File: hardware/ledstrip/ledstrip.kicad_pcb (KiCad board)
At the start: 4 copper layers, 107 x 107.5 mm, 144 parts, among them J1 Conn_ARM_JTAG_SWD_10, J2 USB_C_Receptacle_USB2.0_16P, J4 BMS connectors, J5 Ledstrip connector, J6 Header for STUSB4500 I2C, Q1 Q_NMOS, Q10 Q_PMOS, Q11 Q_NMOS, Q2 Q_NMOS, Q3 Q_NMOS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

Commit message: Fix DRC
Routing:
- net Net-(SW1-B): track 0.43 -> 3.57 mm
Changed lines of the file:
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@@
 		(tags "capacitor")
 		(property "Reference" "C24"
-			(at 0 -1.43 270)
+			(at 0 1.4008 270)
 			(layer "F.SilkS")
 			(effects
@@
 		(layer "F.Cu")
 		(net 116)
+	)
+	(segment
+		(start 182.2927 109.8569)
+		(end 182.5752 110.1394)
+		(width 0.2)
+		(layer "F.Cu")
+		(net 116)
+	)
+	(segment
+		(start 179.5526 109.8569)
+		(end 182.2927 109.8569)
+		(width 0.2)
+		(layer "F.Cu")
+		(net 116)

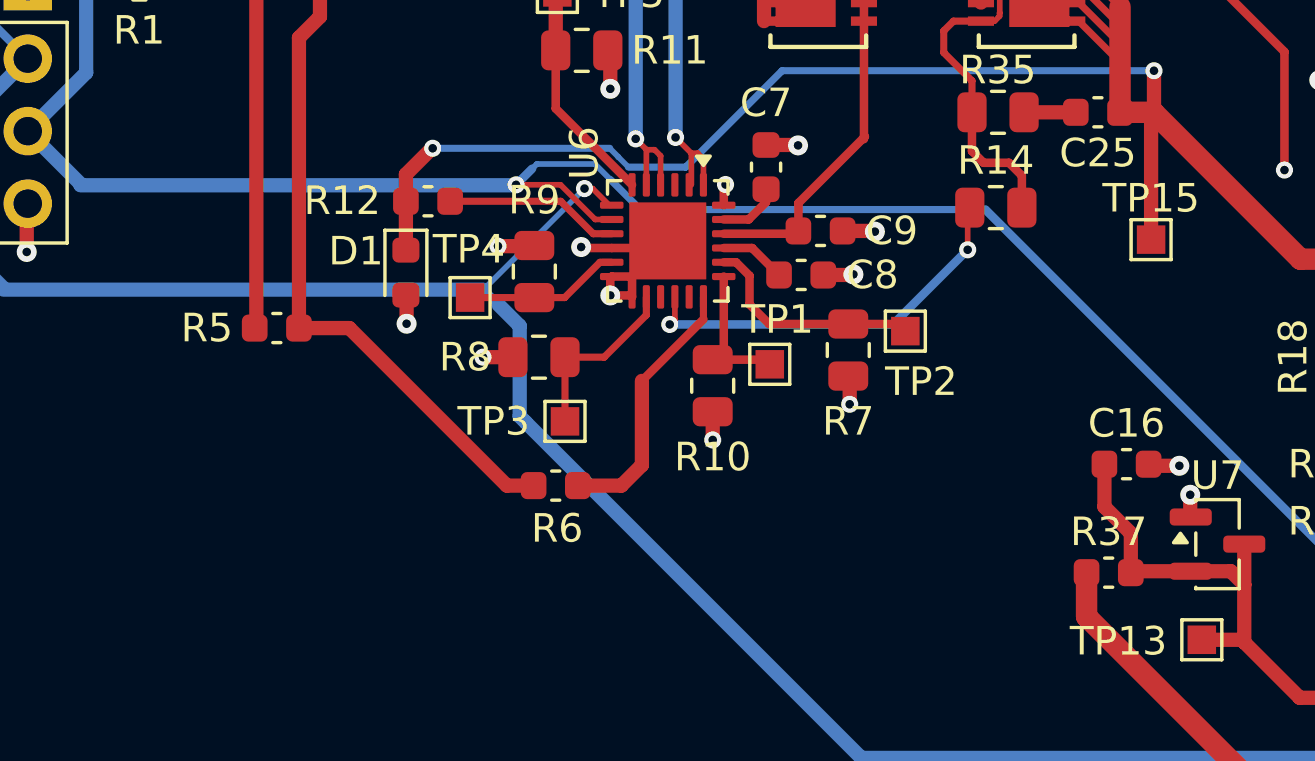
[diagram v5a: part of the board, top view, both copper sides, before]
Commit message: Fix wrong footprint (C_0603 instead of R_0603)
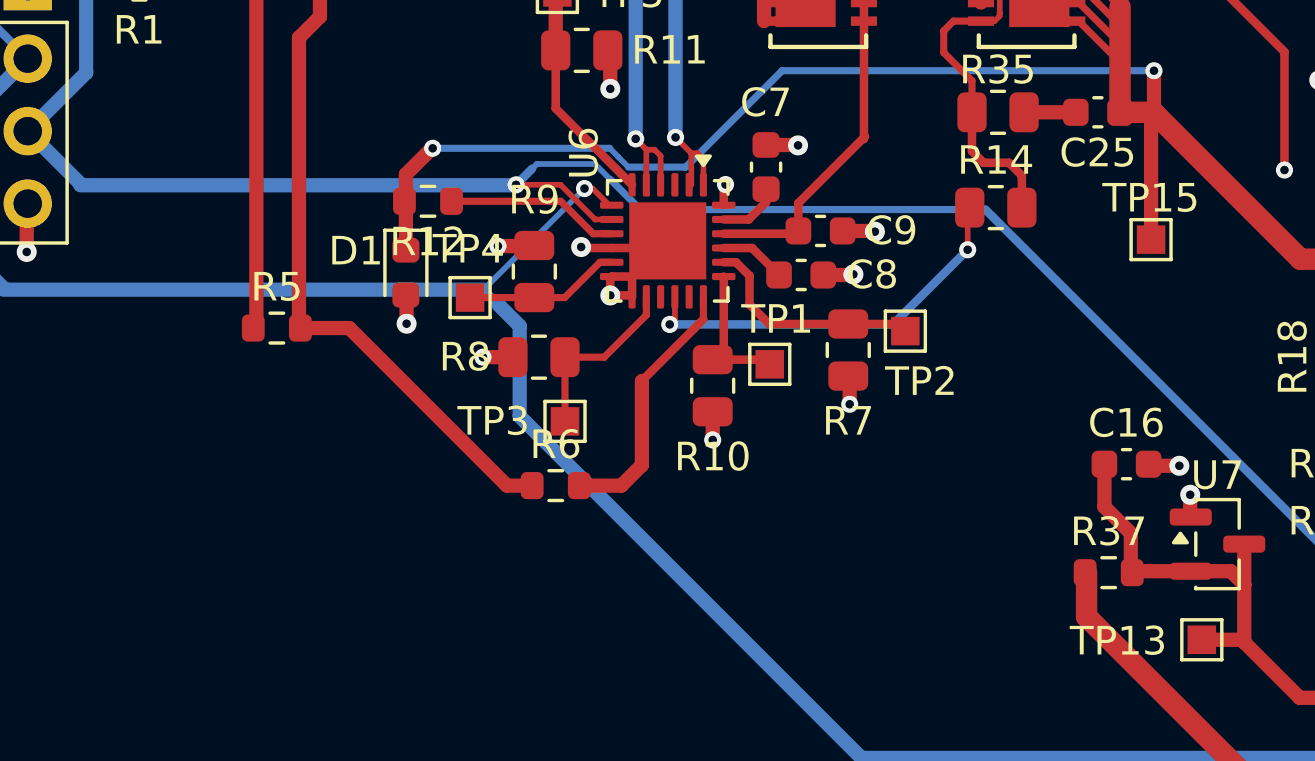
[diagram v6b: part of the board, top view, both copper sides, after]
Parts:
- R12, R37, R5, R6: footprint Capacitor_SMD:C_0603_1608Metric -> Resistor_SMD:R_0603_1608Metric
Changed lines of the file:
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@@
 		)
 	)
-	(footprint "Capacitor_SMD:C_0603_1608Metric"
+	(footprint "Resistor_SMD:R_0603_1608Metric"
 		(layer "F.Cu")
 		(at 119.5 131.25)
-		(descr "Capacitor SMD 0603 (1608 Metric), square (rectangular) end terminal, IPC-7351 nominal, (Body size source: IPC-SM-782 page 76, https://www.pcb-3d.com/wordpress/wp-content/uploads/ipc-sm-782a_amendment_1_and_2.pdf), generated with kicad-footprint-generator")
-		(tags "capacitor")
+		(descr "Resistor SMD 0603 (1608 Metric), square (rectangular) end terminal, IPC-7351 nominal, (Body size source: IPC-SM-782 page 72, https://www.pcb-3d.com/wordpress/wp-content/uploads/ipc-sm-782a_amendment_1_and_2.pdf), generated with kicad-footprint-generator")
+		(tags "resistor")
 		(property "Reference" "R6"
-			(at 0.05 1.5 0)
+			(at 0 -1.43 0)
 			(layer "F.SilkS")
 			(effects
@@
 		(attr smd)
 		(fp_line
-			(start -0.14058 -0.51)
-			(end 0.14058 -0.51)
+			(start -0.237258 -0.5225)
+			(end 0.237258 -0.5225)
 			(stroke
 				(width 0.12)
@@
 		)
 		(fp_line
-			(start -0.14058 0.51)
-			(end 0.14058 0.51)
+			(start -0.237258 0.5225)
+			(end 0.237258 0.5225)
 			(stroke
 				(width 0.12)
@@
 		)
 		(fp_rect
-			(start -0.8 -0.4)
-			(end 0.8 0.4)
+			(start -0.8 -0.4125)
+			(end 0.8 0.4125)
 			(stroke
 				(width 0.1)
@@
 		)
 		(pad "1" smd roundrect
-			(at -0.775 0)
-			(size 0.9 0.95)
+			(at -0.825 0)
+			(size 0.8 0.95)
 			(layers "F.Cu" "F.Mask" "F.Paste")
 			(roundrect_rratio 0.25)
@@
 		)
 		(pad "2" smd roundrect
-			(at 0.775 0)
-			(size 0.9 0.95)
+			(at 0.825 0)
+			(size 0.8 0.95)
 			(layers "F.Cu" "F.Mask" "F.Paste")
 			(roundrect_rratio 0.25)
@@
 		)
 		(embedded_fonts no)
-		(model "${KICAD9_3DMODEL_DIR}/Capacitor_SMD.3dshapes/C_0603_1608Metric.step"
+		(model "${KICAD9_3DMODEL_DIR}/Resistor_SMD.3dshapes/R_0603_1608Metric.step"
 			(offset
 				(xyz 0 0 0)
@@
 		)
 	)
-	(footprint "Capacitor_SMD:C_0603_1608Metric"
+	(footprint "Resistor_SMD:R_0603_1608Metric"
 		(layer "F.Cu")
 		(at 115.025 121.2875 180)
-		(descr "Capacitor SMD 0603 (1608 Metric), square (rectangular) end terminal, IPC-7351 nominal, (Body size source: IPC-SM-782 page 76, https://www.pcb-3d.com/wordpress/wp-content/uploads/ipc-sm-782a_amendment_1_and_2.pdf), generated with kicad-footprint-generator")
-		(tags "capacitor")
+		(descr "Resistor SMD 0603 (1608 Metric), square (rectangular) end terminal, IPC-7351 nominal, (Body size source: IPC-SM-782 page 72, https://www.pcb-3d.com/wordpress/wp-content/uploads/ipc-sm-782a_amendment_1_and_2.pdf), generated with kicad-footprint-generator")
+		(tags "resistor")
 		(property "Reference" "R12"
-			(at 3.005 0.0175 0)
+			(at 0 -1.43 180)
 			(layer "F.SilkS")
 			(effects
@@
 		)
 		(property "Value" "1k"
-			(at 0 1.43 0)
+			(at 0 1.43 180)
 			(layer "F.Fab")
 			(effects
@@
 		)
 		(property "Datasheet" "https://www.vishay.com/doc?20037"
-			(at 0 0 0)
+			(at 0 0 180)
 			(layer "F.Fab")
 			(hide yes)
@@
 		)
 		(property "Description" "Resistor"
-			(at 0 0 0)
+			(at 0 0 180)
 			(layer "F.Fab")
 			(hide yes)
@@
 		(attr smd)
 		(fp_line
-			(start -0.14058 0.51)
-			(end 0.14058 0.51)
+			(start -0.237258 0.5225)
+			(end 0.237258 0.5225)
 			(stroke
 				(width 0.12)
@@
 		)
 		(fp_line
-			(start -0.14058 -0.51)
-			(end 0.14058 -0.51)
+			(start -0.237258 -0.5225)
+			(end 0.237258 -0.5225)
 			(stroke
 				(width 0.12)
@@
 		)
 		(fp_rect
-			(start -0.8 -0.4)
-			(end 0.8 0.4)
+			(start -0.8 -0.4125)
+			(end 0.8 0.4125)
 			(stroke
 				(width 0.1)
@@
 		)
 		(fp_text user "${REFERENCE}"
-			(at 0 0 0)
+			(at 0 0 180)
 			(layer "F.Fab")
 			(effects
@@
 		)
 		(pad "1" smd roundrect
-			(at -0.775 0 180)
-			(size 0.9 0.95)
+			(at -0.825 0 180)
+			(size 0.8 0.95)
 			(layers "F.Cu" "F.Mask" "F.Paste")
 			(roundrect_rratio 0.25)
@@
 		)
 		(pad "2" smd roundrect
-			(at 0.775 0 180)
-			(size 0.9 0.95)
+			(at 0.825 0 180)
+			(size 0.8 0.95)
 			(layers "F.Cu" "F.Mask" "F.Paste")
 			(roundrect_rratio 0.25)
@@
 		)
 		(embedded_fonts no)
-		(model "${KICAD9_3DMODEL_DIR}/Capacitor_SMD.3dshapes/C_0603_1608Metric.step"
+		(model "${KICAD9_3DMODEL_DIR}/Resistor_SMD.3dshapes/R_0603_1608Metric.step"
 			(offset
 				(xyz 0 0 0)
@@
 		)
 	)
-	(footprint "Capacitor_SMD:C_0603_1608Metric"
+	(footprint "Resistor_SMD:R_0603_1608Metric"
 		(layer "F.Cu")
 		(at 138.875 134.3)
-		(descr "Capacitor SMD 0603 (1608 Metric), square (rectangular) end terminal, IPC-7351 nominal, (Body size source: IPC-SM-782 page 76, https://www.pcb-3d.com/wordpress/wp-content/uploads/ipc-sm-782a_amendment_1_and_2.pdf), generated with kicad-footprint-generator")
-		(tags "capacitor")
+		(descr "Resistor SMD 0603 (1608 Metric), square (rectangular) end terminal, IPC-7351 nominal, (Body size source: IPC-SM-782 page 72, https://www.pcb-3d.com/wordpress/wp-content/uploads/ipc-sm-782a_amendment_1_and_2.pdf), generated with kicad-footprint-generator")
+		(tags "resistor")
 		(property "Reference" "R37"
 			(at 0 -1.43 0)
@@
 		(attr smd)
 		(fp_line
-			(start -0.14058 -0.51)
-			(end 0.14058 -0.51)
+			(start -0.237258 -0.5225)
+			(end 0.237258 -0.5225)
 			(stroke
 				(width 0.12)
@@
 		)
 		(fp_line
-			(start -0.14058 0.51)
-			(end 0.14058 0.51)
+			(start -0.237258 0.5225)
+			(end 0.237258 0.5225)
 			(stroke
 				(width 0.12)
@@
 		)
 		(fp_rect
-			(start -0.8 -0.4)
-			(end 0.8 0.4)
+			(start -0.8 -0.4125)
+			(end 0.8 0.4125)
 			(stroke
 				(width 0.1)
@@
 		)
 		(pad "1" smd roundrect
-			(at -0.775 0)
-			(size 0.9 0.95)
+			(at -0.825 0)
+			(size 0.8 0.95)
 			(layers "F.Cu" "F.Mask" "F.Paste")
 			(roundrect_rratio 0.25)
@@
 		)
 		(pad "2" smd roundrect
-			(at 0.775 0)
-			(size 0.9 0.95)
+			(at 0.825 0)
+			(size 0.8 0.95)
 			(layers "F.Cu" "F.Mask" "F.Paste")
 			(roundrect_rratio 0.25)
@@
 		)
 		(embedded_fonts no)
-		(model "${KICAD9_3DMODEL_DIR}/Capacitor_SMD.3dshapes/C_0603_1608Metric.step"
+		(model "${KICAD9_3DMODEL_DIR}/Resistor_SMD.3dshapes/R_0603_1608Metric.step"
 			(offset
 				(xyz 0 0 0)
@@
 		)
 	)
-	(footprint "Capacitor_SMD:C_0603_1608Metric"
+	(footprint "Resistor_SMD:R_0603_1608Metric"
 		(layer "F.Cu")
 		(at 109.728 125.73)
-		(descr "Capacitor SMD 0603 (1608 Metric), square (rectangular) end terminal, IPC-7351 nominal, (Body size source: IPC-SM-782 page 76, https://www.pcb-3d.com/wordpress/wp-content/uploads/ipc-sm-782a_amendment_1_and_2.pdf), generated with kicad-footprint-generator")
-		(tags "capacitor")
+		(descr "Resistor SMD 0603 (1608 Metric), square (rectangular) end terminal, IPC-7351 nominal, (Body size source: IPC-SM-782 page 72, https://www.pcb-3d.com/wordpress/wp-content/uploads/ipc-sm-782a_amendment_1_and_2.pdf), generated with kicad-footprint-generator")
+		(tags "resistor")
 		(property "Reference" "R5"
-			(at -2.45 0 0)
+			(at 0 -1.43 0)
 			(layer "F.SilkS")
 			(effects
@@
 		(attr smd)
 		(fp_line
-			(start -0.14058 -0.51)
-			(end 0.14058 -0.51)
+			(start -0.237258 -0.5225)
+			(end 0.237258 -0.5225)
 			(stroke
 				(width 0.12)
@@
 		)
 		(fp_line
-			(start -0.14058 0.51)
-			(end 0.14058 0.51)
+			(start -0.237258 0.5225)
+			(end 0.237258 0.5225)
 			(stroke
 				(width 0.12)
@@
 		)
 		(fp_rect
-			(start -0.8 -0.4)
-			(end 0.8 0.4)
+			(start -0.8 -0.4125)
+			(end 0.8 0.4125)
 			(stroke
 				(width 0.1)
@@
 		)
 		(pad "1" smd roundrect
-			(at -0.775 0)
-			(size 0.9 0.95)
+			(at -0.825 0)
+			(size 0.8 0.95)
 			(layers "F.Cu" "F.Mask" "F.Paste")
 			(roundrect_rratio 0.25)
@@
 		)
 		(pad "2" smd roundrect
-			(at 0.775 0)
-			(size 0.9 0.95)
+			(at 0.825 0)
+			(size 0.8 0.95)
 			(layers "F.Cu" "F.Mask" "F.Paste")
 			(roundrect_rratio 0.25)
@@
 		)
 		(embedded_fonts no)
-		(model "${KICAD9_3DMODEL_DIR}/Capacitor_SMD.3dshapes/C_0603_1608Metric.step"
+		(model "${KICAD9_3DMODEL_DIR}/Resistor_SMD.3dshapes/R_0603_1608Metric.step"
 			(offset
 				(xyz 0 0 0)
